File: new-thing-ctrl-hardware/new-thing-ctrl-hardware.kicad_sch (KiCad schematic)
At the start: 43 parts, among them J1 MSTBAish, J10 MSTBAish, J11 Neopixels, J2 MSTBAish, J3 SD, J4 MFRC522, J5 Conn_01x04_Male, J6 Screw_Terminal_01x09, J7 LCD, J8 Screw_Terminal_01x06, J9 Screw_Terminal_01x06, Q1 TIP120, Q2 TIP120, SW1 6X6, SW2 6X6, SW3 6X6, SW4 6X6, U1 L7805, U2 Pico

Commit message: routed
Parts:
- added C8: 100n, Capacitor_THT:C_Disc_D7.0mm_W2.5mm_P5.00mm, symbol Device:C_Small
- added C9: 10u, Capacitor_THT:CP_Radial_D5.0mm_P2.50mm, symbol machine-controller-rescue:CP_Small-Device
- SW1, SW2, SW3, SW4: footprint Button_Switch_THT:SW_PUSH_6mm_H7.3mm -> Button_Switch_THT:SW_PUSH_6mm_H13mm
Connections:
- net SPI_CLK is gone; now on net SPI_SCK: J3.4 (Pin_4)
- net +3V3: no longer D5.1 (VDD), J11.3 (Pin_3)
- net +5V: now also D5.1 (VDD), J11.3 (Pin_3), C8.1, C9.1
- net ADC_0: now also J6.5 (Pin_5); no longer J6.7 (Pin_7)
- net ADC_1: no longer J6.5 (Pin_5)
- net ADC_2: now also J6.7 (Pin_7)
- net BUT_0: now also U2.15 (GPIO11); no longer U2.1 (GPIO0)
- net BUT_1: now also U2.14 (GPIO10); no longer U2.2 (GPIO1)
- net BUT_2: now also U2.17 (GPIO13); no longer U2.4 (GPIO2)
- net BUT_3: now also U2.16 (GPIO12); no longer U2.5 (GPIO3)
- net COIL_0: now also U2.10 (GPIO7); no longer U2.16 (GPIO12)
- net COIL_1: now also U2.11 (GPIO8); no longer U2.17 (GPIO13)
- net GND: now also C8.2, C9.2
- net LCD_BACKLIGHT: now also U2.5 (GPIO3); no longer U2.14 (GPIO10)
- net LCD_DC/RS: now also U2.4 (GPIO2); no longer U2.12 (GPIO9)
- net LCD_RST: now also U2.2 (GPIO1); no longer U2.11 (GPIO8)
- net NEOPIXEL: now also U2.12 (GPIO9); no longer U2.29 (GPIO22)
- net NFC_IRQ: no longer U2.15 (GPIO11)
- net NFC_RST: now also U2.22 (GPIO17); no longer U2.26 (GPIO20)
- net SPI_CS_LCD: now also U2.1 (GPIO0); no longer U2.22 (GPIO17)
- net SPI_CS_SD: now also U2.9 (GPIO6)
- net SPI_CS_TCH: now also U2.29 (GPIO22); no longer U2.9 (GPIO6)
- net SPI_RX: now also J8.2 (Pin_2); no longer J8.3 (Pin_3)
- net SPI_SCK: now also J8.3 (Pin_3); no longer J8.2 (Pin_2)
- net TCH_IRQ: now also U2.26 (GPIO20); no longer U2.10 (GPIO7)
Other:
- moved on the sheet: C1, C2, C3, C4, C5, C6, C7, D1, D3, D4, D5, D6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

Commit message: ready for review and manufacture
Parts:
- removed J4: MFRC522, Connector_JST:JST_XH_S8B-XH-A_1x08_P2.50mm_Horizontal, symbol Connector:Conn_01x08_Male
- removed J6: Screw_Terminal_01x09, Connector_Phoenix_MSTB:PhoenixContact_MSTBA_2,5_9-G-5,08_1x09_P5.08mm_Horizontal, symbol Connector:Screw_Terminal_01x09
- added J12: EXP1, Connector_Phoenix_MSTB:PhoenixContact_MSTBA_2,5_6-G-5,08_1x06_P5.08mm_Horizontal, symbol Connector:Screw_Terminal_01x06
- added J4: PN532, Connector_JST:JST_XH_S4B-XH-A_1x04_P2.50mm_Horizontal, symbol Connector:Conn_01x04_Male
- added J6: EXP0, Connector_Phoenix_MSTB:PhoenixContact_MSTBA_2,5_6-G-5,08_1x06_P5.08mm_Horizontal, symbol Connector:Screw_Terminal_01x06
- added R5, R6: 100K, Resistor_THT:R_Axial_DIN0204_L3.6mm_D1.6mm_P7.62mm_Horizontal, symbol Device:R_Small
- J5: footprint Connector_JST:JST_XH_B4B-XH-A_1x04_P2.50mm_Vertical -> Connector_JST:JST_XH_S4B-XH-A_1x04_P2.50mm_Horizontal
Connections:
- net SPI_CS_NFC is gone; now on net SPI_CS_TCH: U2.27 (GPIO21)
- net +3V3: now also J12.5 (Pin_5), J4.2 (Pin_2), J6.5 (Pin_5)
- net +5V: now also J12.6 (Pin_6), J6.6 (Pin_6)
- net ADC_0: now also J6.2 (Pin_2)
- net ADC_1: now also J6.3 (Pin_3)
- net ADC_2: now also J6.4 (Pin_4)
- net D15: now also J12.4 (Pin_4)
- net GND: now also J12.1 (Pin_1), J4.1 (Pin_1), J6.1 (Pin_1), R5.2, R6.2
- net SCL: now also J4.4 (Pin_4)
- net SDA: now also J4.3 (Pin_3)
- net SPI_CS_TCH: no longer U2.29 (GPIO22)
- net at Q1.1 (B), R7.1: now also R5.1
- net at Q2.1 (B), R3.1: now also R6.1
- net NFC_RST renamed D17
- net D17: now also J12.2 (Pin_2)
- new net D22: J12.3 (Pin_3), U2.29 (GPIO22)
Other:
- moved on the sheet: C6

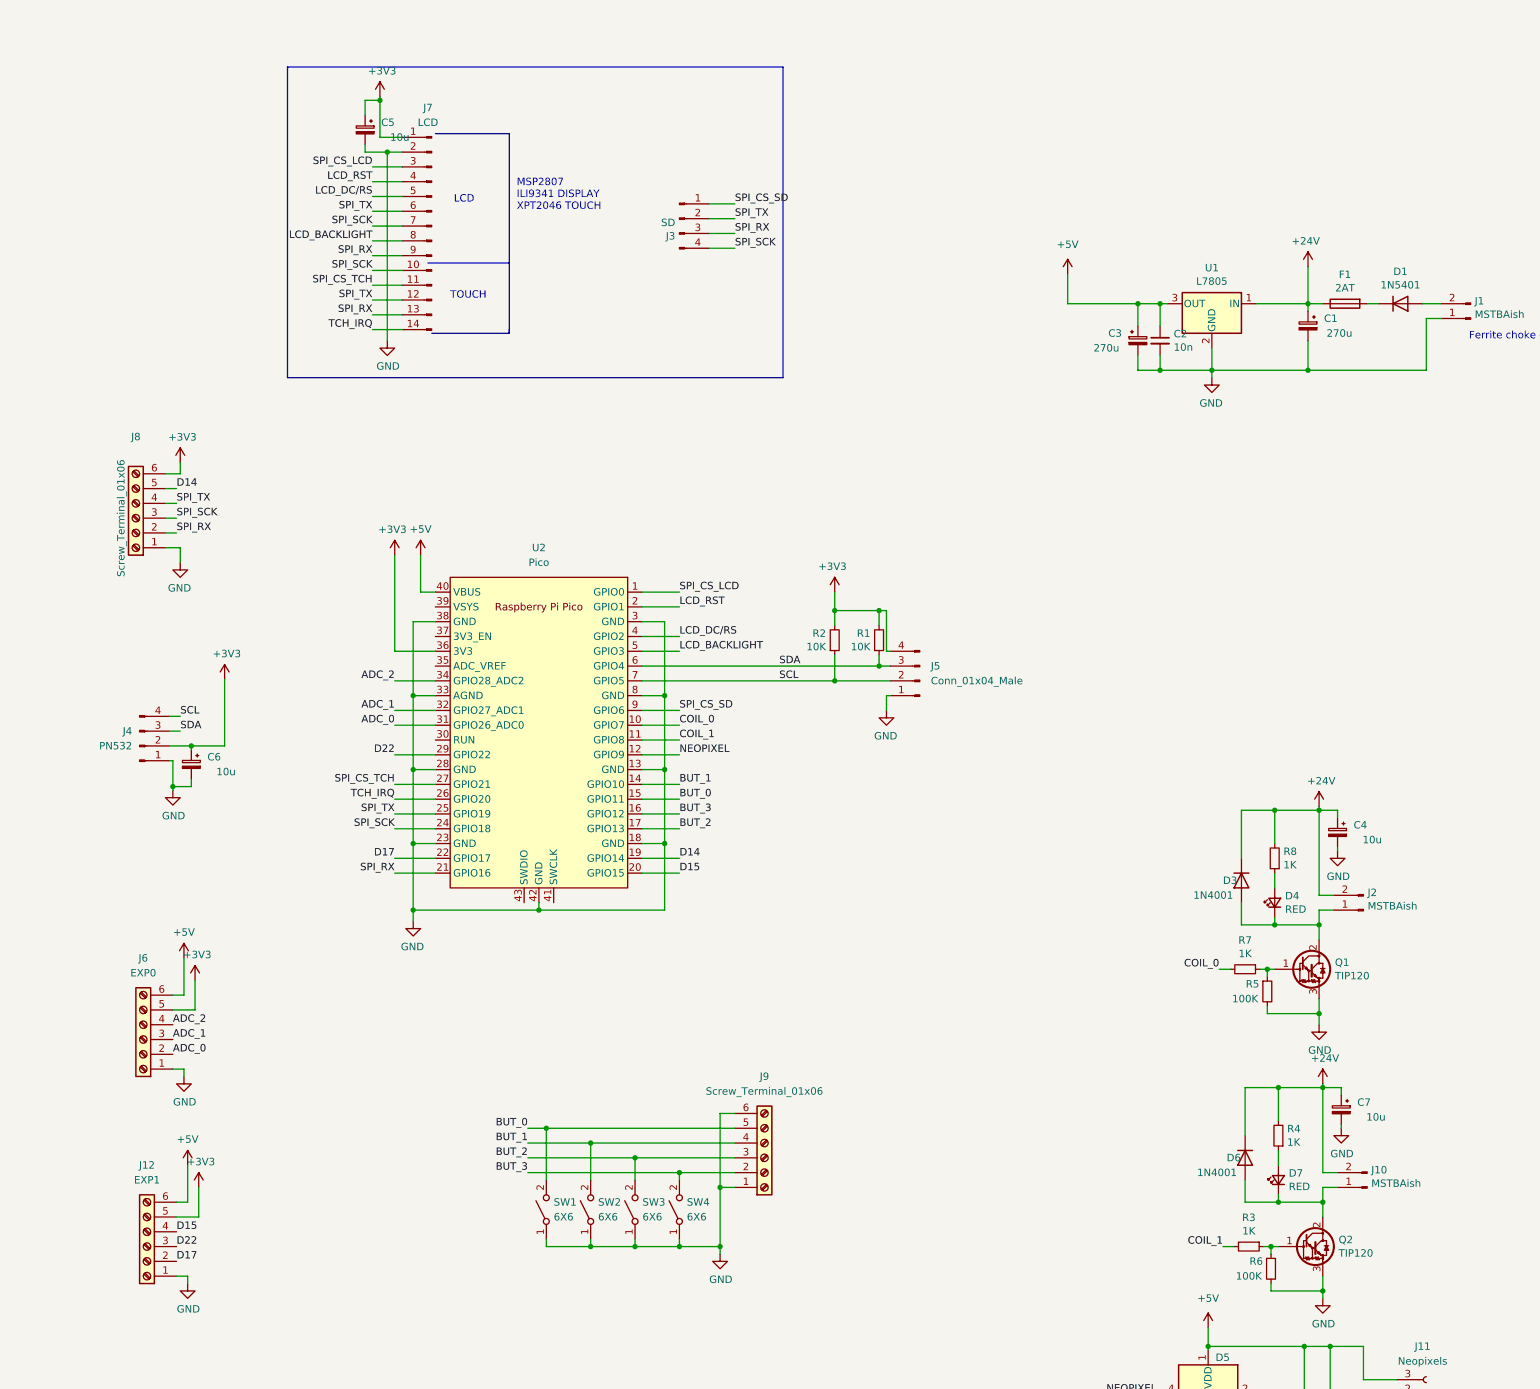
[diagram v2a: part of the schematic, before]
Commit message: changed some connector footprints, added reset button
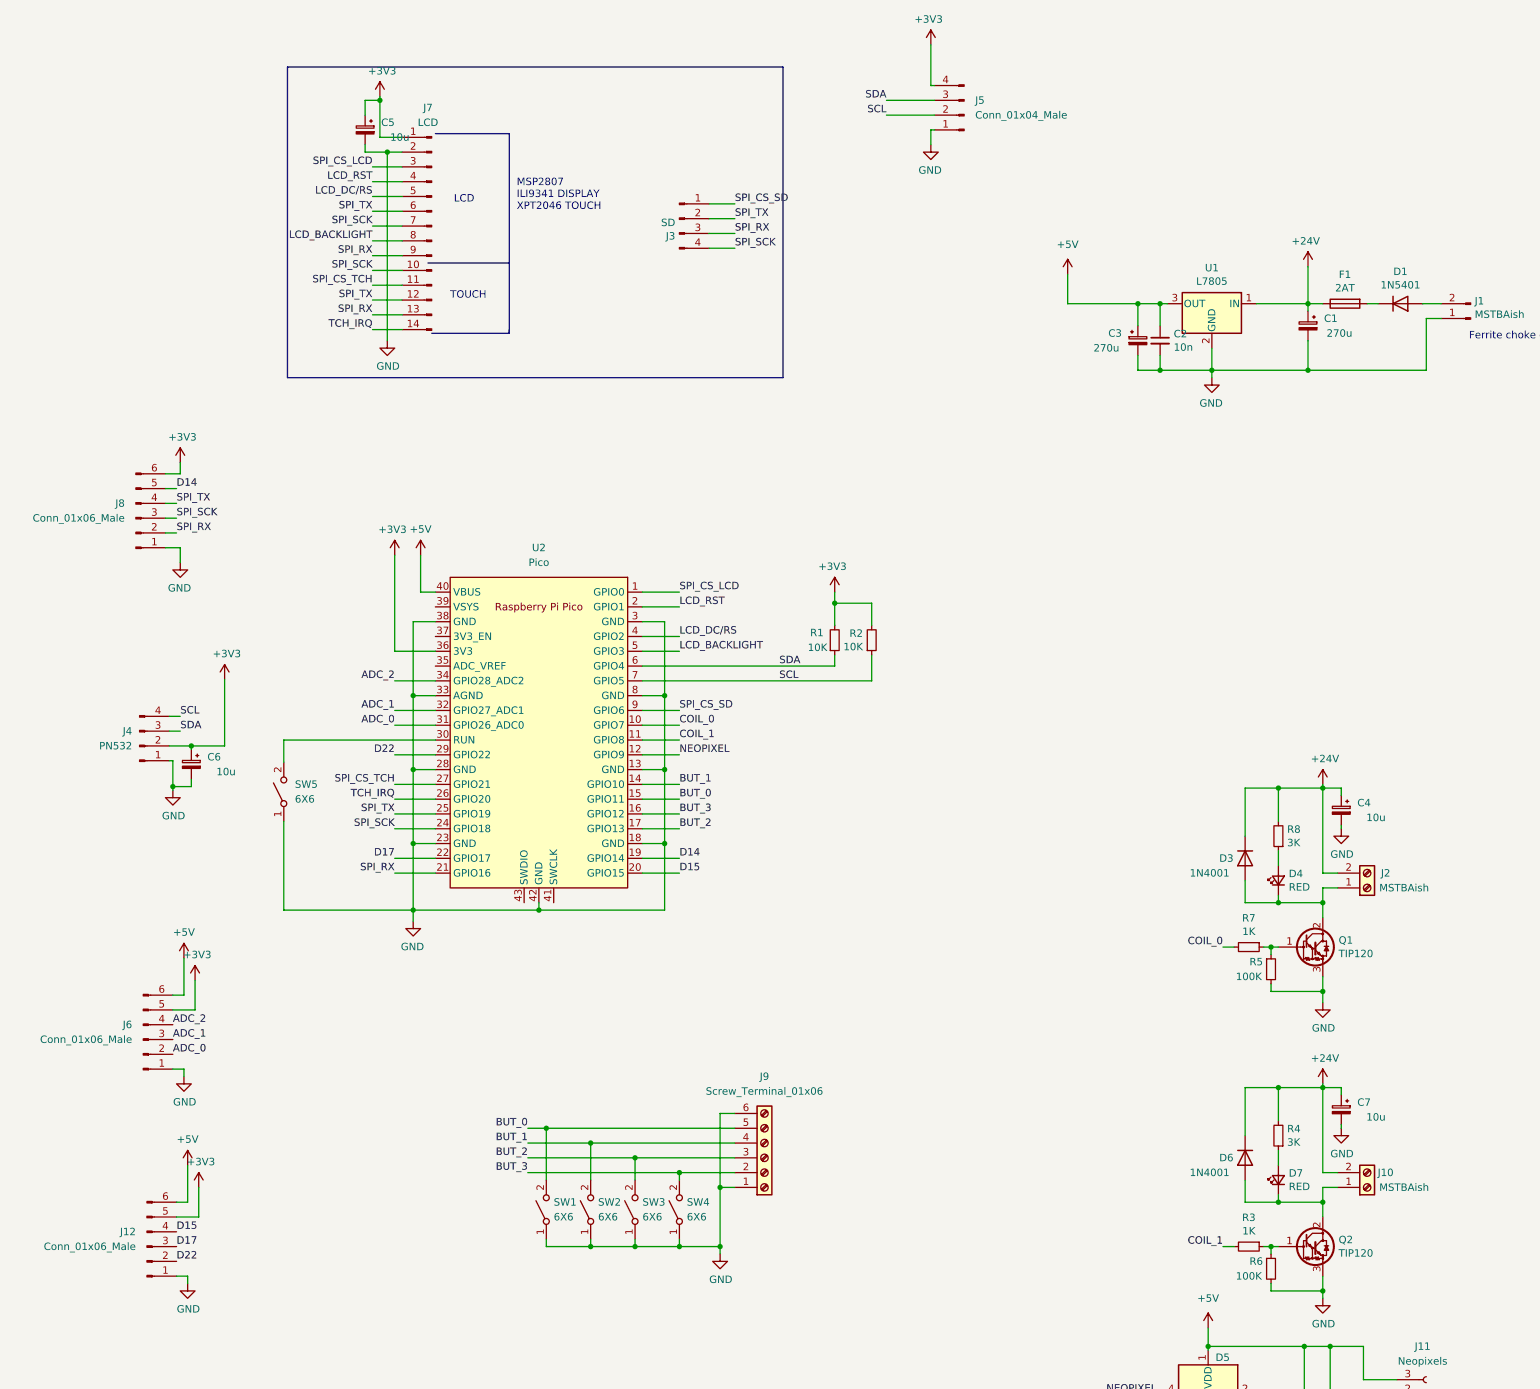
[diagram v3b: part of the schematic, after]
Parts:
- removed J10, J2: MSTBAish, Connector_Phoenix_MSTB:PhoenixContact_MSTBA_2,5_2-G-5,08_1x02_P5.08mm_Horizontal, symbol Connector:Conn_01x02_Male
- removed J12: EXP1, Connector_Phoenix_MSTB:PhoenixContact_MSTBA_2,5_6-G-5,08_1x06_P5.08mm_Horizontal, symbol Connector:Screw_Terminal_01x06
- removed J6: EXP0, Connector_Phoenix_MSTB:PhoenixContact_MSTBA_2,5_6-G-5,08_1x06_P5.08mm_Horizontal, symbol Connector:Screw_Terminal_01x06
- removed J8: Screw_Terminal_01x06, Connector_Phoenix_MSTB:PhoenixContact_MSTBA_2,5_6-G-5,08_1x06_P5.08mm_Horizontal, symbol Connector:Screw_Terminal_01x06
- added J10, J2: MSTBAish, Connector_Phoenix_MSTB:PhoenixContact_MSTBA_2,5_2-G-5,08_1x02_P5.08mm_Horizontal, symbol Connector:Screw_Terminal_01x02
- added J12, J6, J8: Conn_01x06_Male, Connector_JST:JST_XH_S6B-XH-A_1x06_P2.50mm_Horizontal, symbol Connector:Conn_01x06_Male
- added SW5: 6X6, Button_Switch_THT:SW_PUSH_6mm_H4.3mm, symbol Switch:SW_SPST
- R4, R8: value 1K -> 3K
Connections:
- net +24V: now also J10.2 (Pin_2), J2.2 (Pin_2)
- net +3V3: now also J12.5 (Pin_5), J6.5 (Pin_5), J8.6 (Pin_6)
- net +5V: now also J12.6 (Pin_6), J6.6 (Pin_6)
- net ADC_0: now also J6.2 (Pin_2)
- net ADC_1: now also J6.3 (Pin_3)
- net ADC_2: now also J6.4 (Pin_4)
- net D14: now also J8.5 (Pin_5)
- net D15: now also J12.4 (Pin_4)
- net D17: now also J12.3 (Pin_3)
- net D22: now also J12.2 (Pin_2)
- net GND: now also J12.1 (Pin_1), J6.1 (Pin_1), J8.1 (Pin_1), SW5.1 (A)
- net SPI_RX: now also J8.2 (Pin_2)
- net SPI_SCK: now also J8.3 (Pin_3)
- net SPI_TX: now also J8.4 (Pin_4)
- net at D3.2 (A), D4.1 (K), Q1.2 (C): now also J2.1 (Pin_1)
- net at D6.2 (A), D7.1 (K), Q2.2 (C): now also J10.1 (Pin_1)
- net at U2.30 (RUN): now also SW5.2 (B)
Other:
- moved on the sheet: C4, D3, D4, J5, Q1, R1, R2, R5, R7, R8
